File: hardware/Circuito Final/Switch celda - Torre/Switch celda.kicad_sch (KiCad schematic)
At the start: 34 parts, among them Q1 MMBT2222A, Q2 MMBT2907A, Q3 MMBT2222A

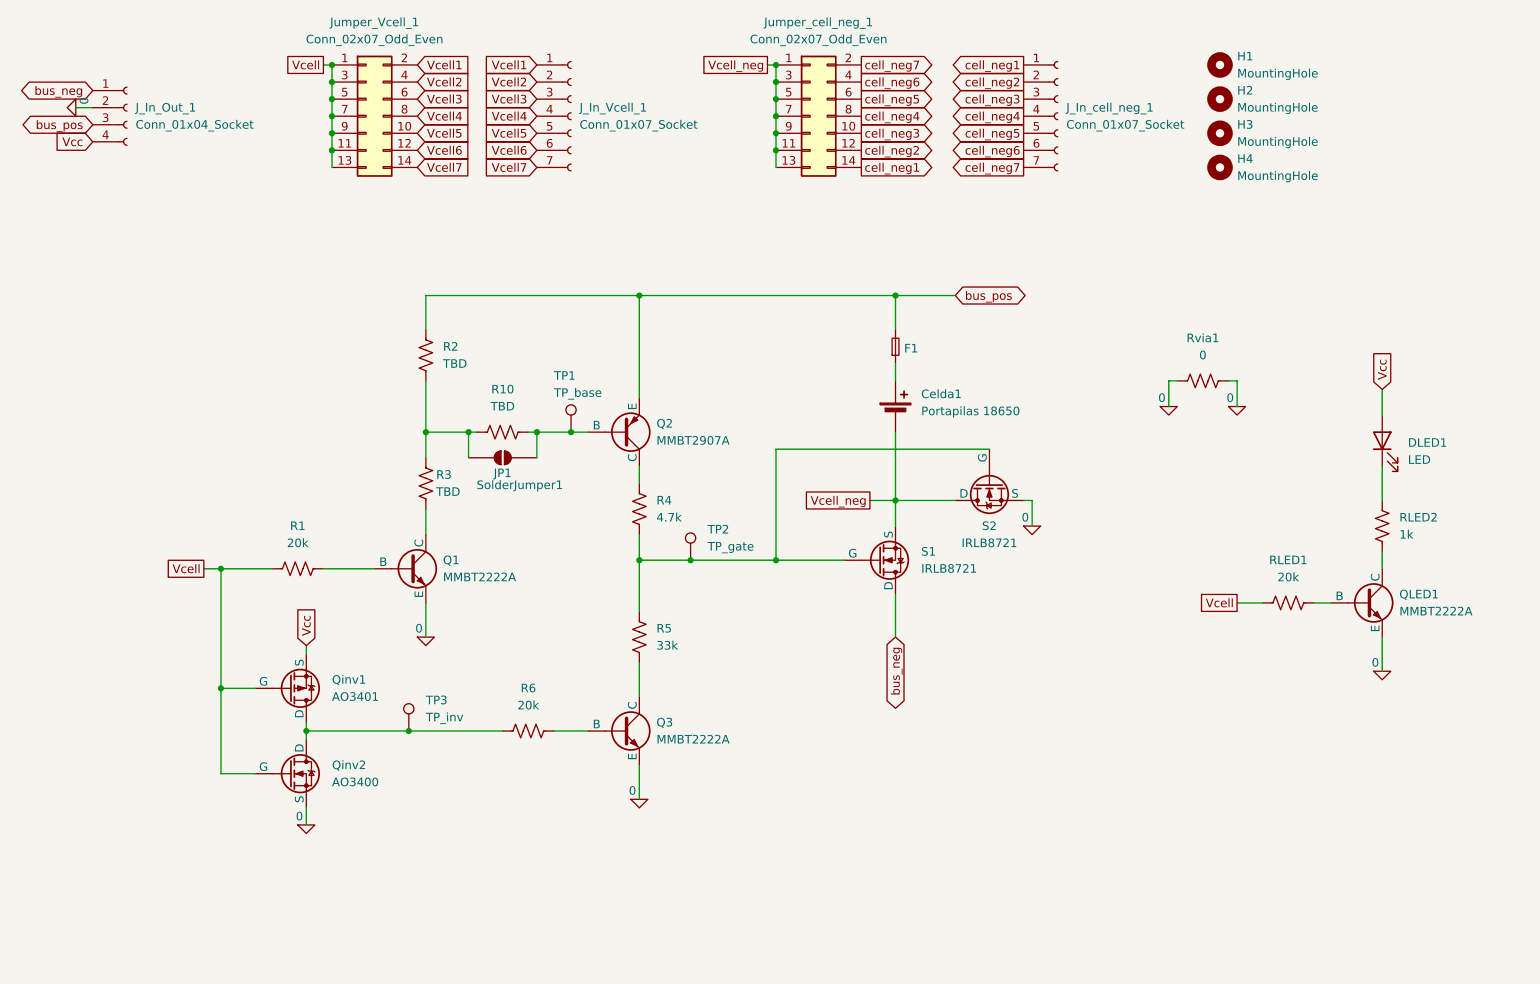
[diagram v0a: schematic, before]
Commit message: clasifica los bloques en el esquematico de kicad
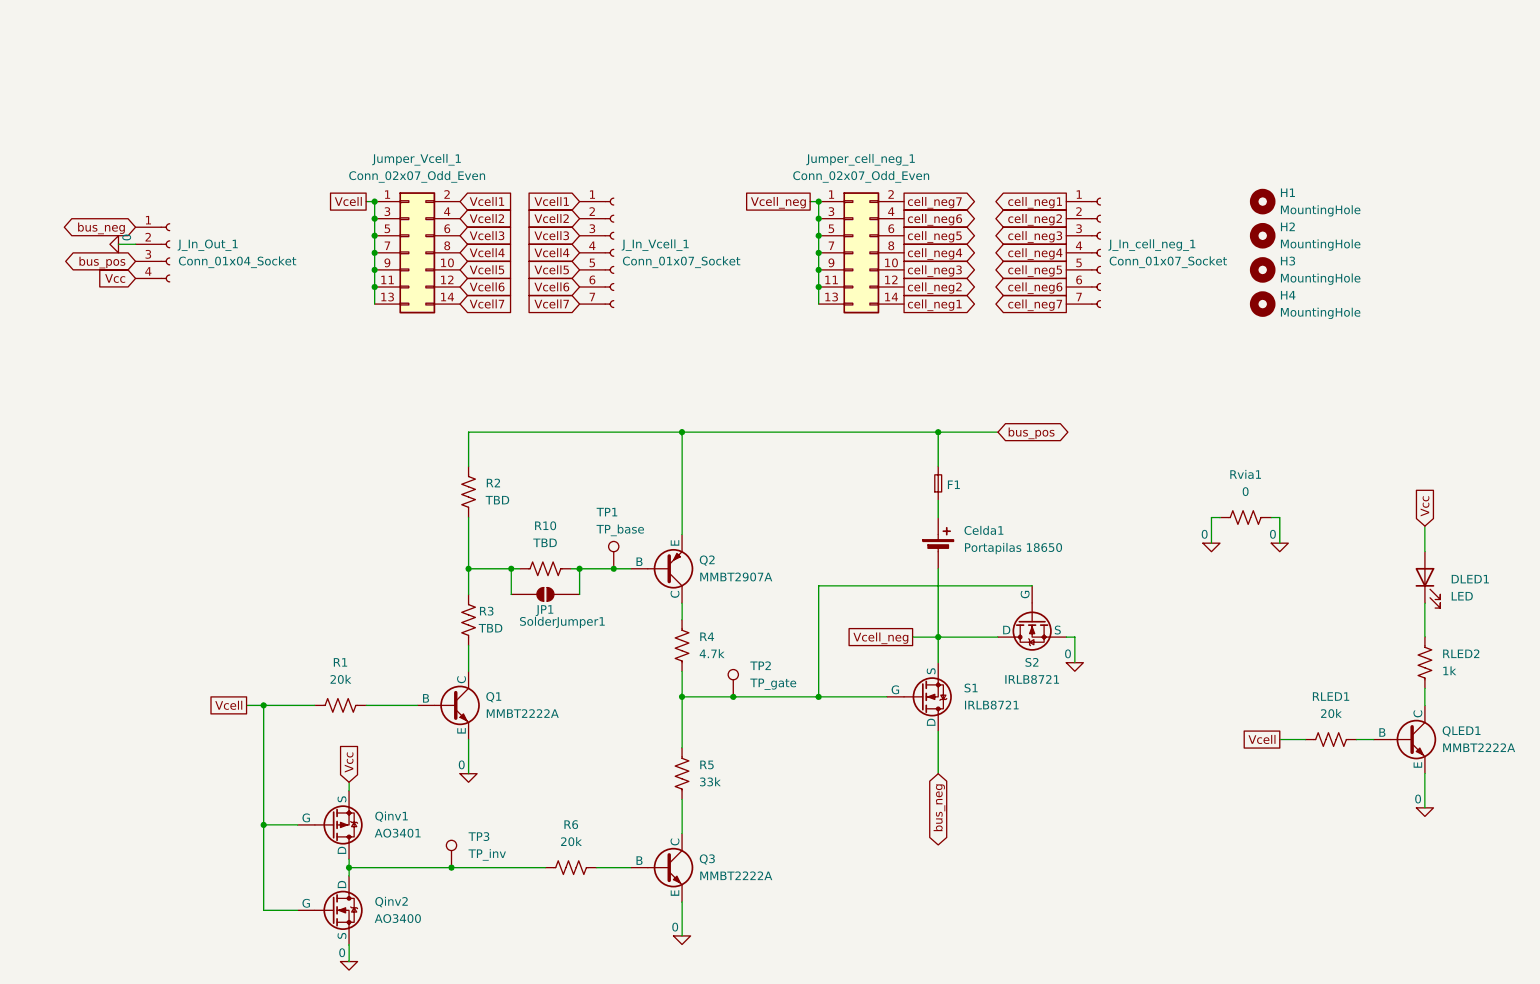
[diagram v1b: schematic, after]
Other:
- moved on the sheet: Celda1, DLED1, F1, H1, H2, H3, H4, JP1, J_In_Out_1, J_In_Vcell_1, J_In_cell_neg_1, Jumper_Vcell_1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
